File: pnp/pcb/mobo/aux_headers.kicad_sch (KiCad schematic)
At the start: 1 part, among them J21 qwiic

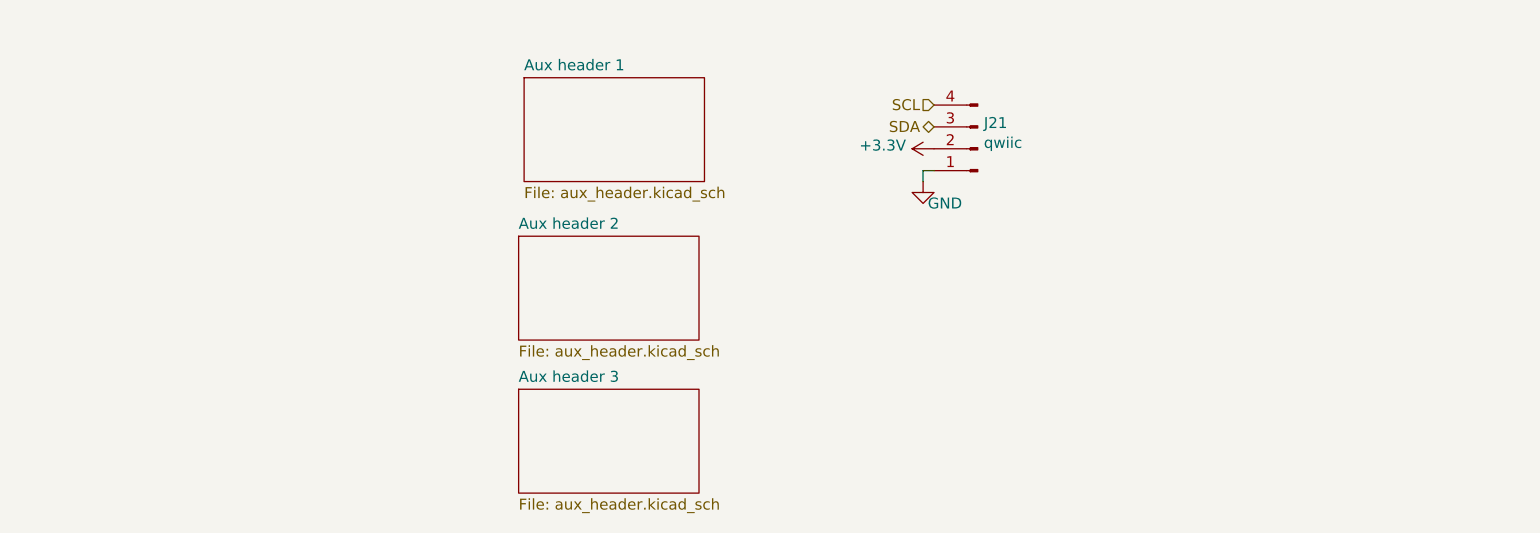
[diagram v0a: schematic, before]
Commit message: All sheets cleaned up
All symbols and their fields are now neatly organized.

All hierarchical pins are already imported,
except for the microcontroller sheet.
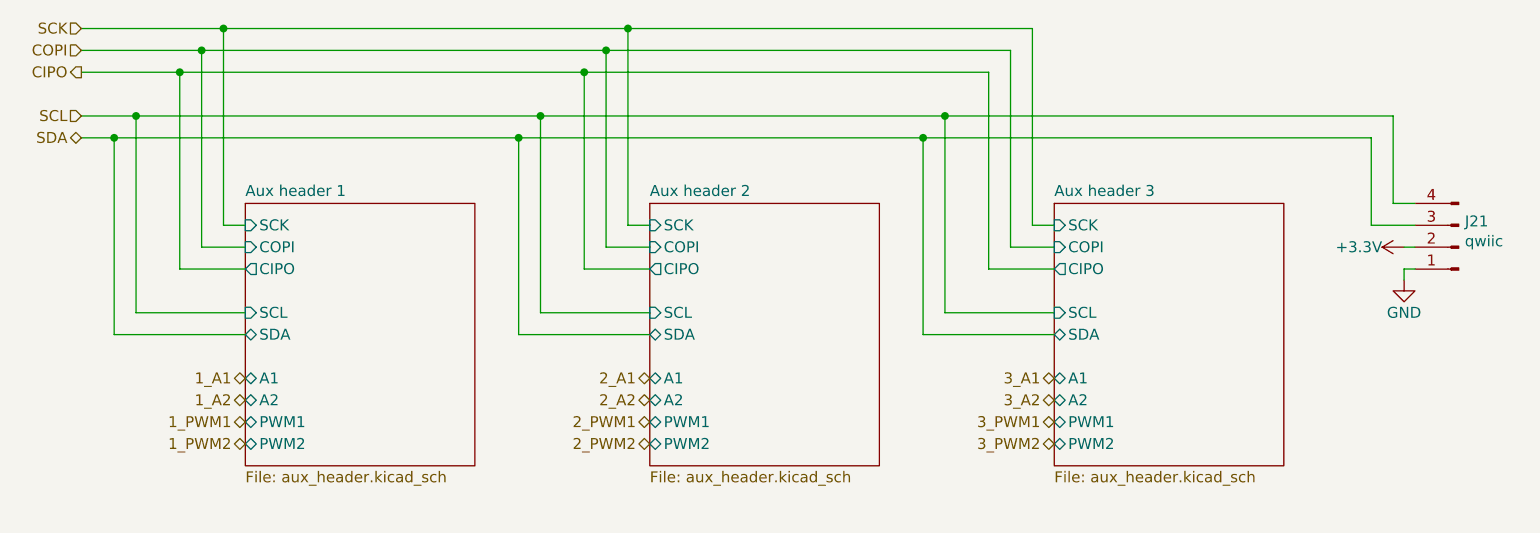
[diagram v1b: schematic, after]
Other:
- sheet Aux header 1 ports: added A1, A2, CIPO, COPI, PWM1, PWM2, SCK, SCL, SDA; removed none
- sheet Aux header 2 ports: added A1, A2, CIPO, COPI, PWM1, PWM2, SCK, SCL, SDA; removed none
- sheet Aux header 3 ports: added A1, A2, CIPO, COPI, PWM1, PWM2, SCK, SCL, SDA; removed none
- moved on the sheet: J21

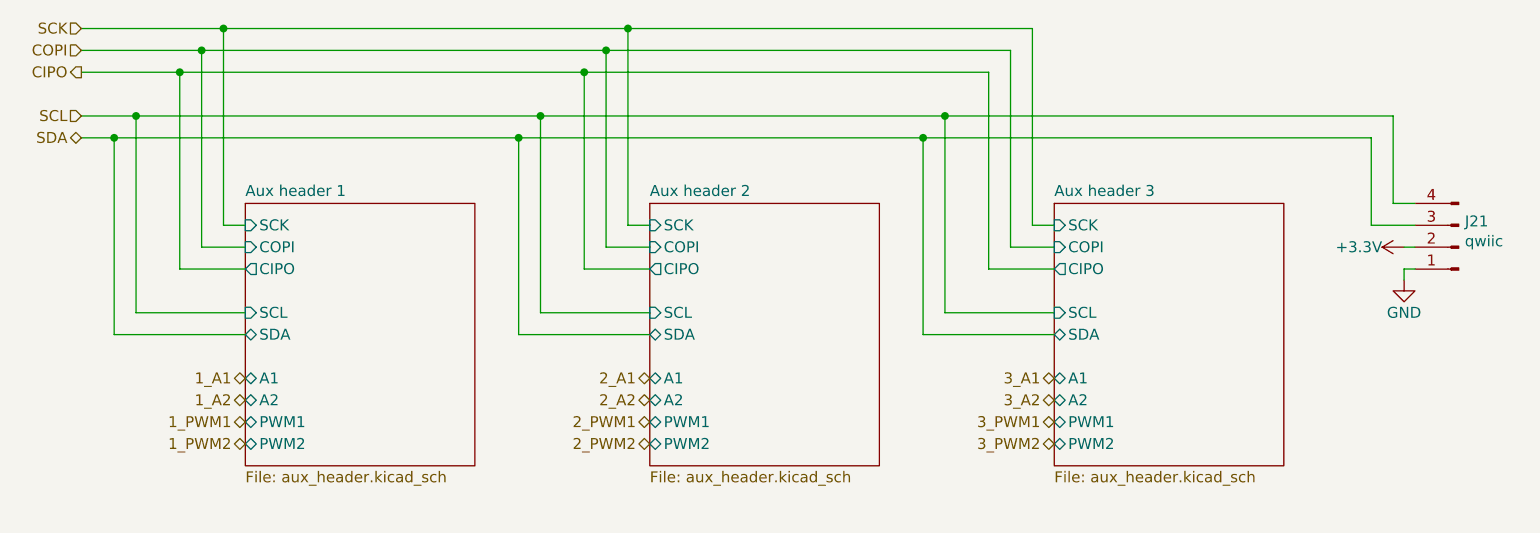
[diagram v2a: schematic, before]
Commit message: moving mobo-rev04b0 into mobo-rev04 branch from old repo
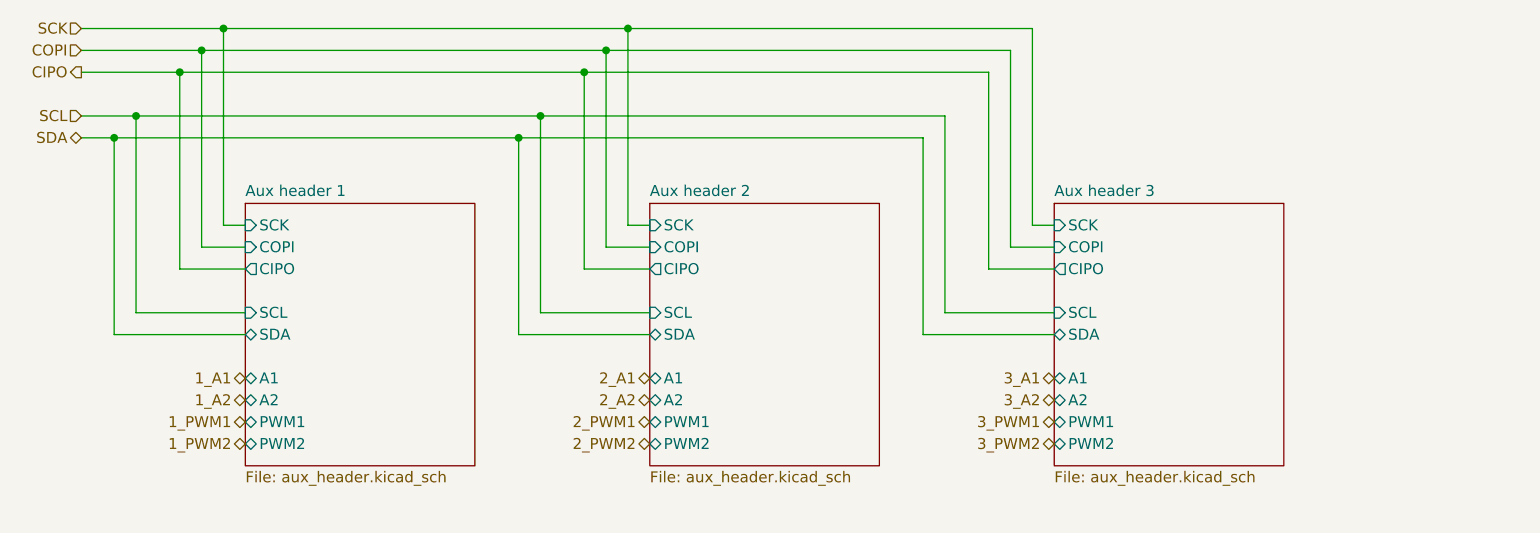
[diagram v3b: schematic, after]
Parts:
- removed J21: qwiic, Connector_JST:JST_SH_BM04B-SRSS-TB_1x04-1MP_P1.00mm_Vertical, symbol Connector:Conn_01x04_Male
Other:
- company: (none) -> Opulo
- title: Output -> LumenPnP Motherboard
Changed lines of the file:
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@@
   (paper "A4")
   (title_block
-    (title "Output")
+    (title "LumenPnP Motherboard")
     (date "2022-03-29")
     (rev "003")
-  )
-  (junction (at 171.45 81.28) (diameter 0) (color 0 0 0 0)
+    (company "Opulo")
   )
   (junction (at 85.09 73.66) (diameter 0) (color 0 0 0 0)
@@
   (junction (at 90.17 68.58) (diameter 0) (color 0 0 0 0)
   )
-  (junction (at 173.99 78.74) (diameter 0) (color 0 0 0 0)
-  )
   (wire (pts (xy 90.17 91.44) (xy 90.17 68.58))
     (stroke (width 0) (type default) (color 0 0 0 0))
@@
     (stroke (width 0) (type default) (color 0 0 0 0))
   )
-  (wire (pts (xy 227.33 97.79) (xy 227.33 96.52))
-    (stroke (width 0) (type default) (color 0 0 0 0))
-  )
   (wire (pts (xy 90.17 91.44) (xy 92.71 91.44))
     (stroke (width 0) (type default) (color 0 0 0 0))
@@
     (stroke (width 0) (type default) (color 0 0 0 0))
   )
-  (wire (pts (xy 226.06 88.9) (xy 226.06 78.74))
-    (stroke (width 0) (type default) (color 0 0 0 0))
-  )
   (wire (pts (xy 137.16 91.44) (xy 137.16 68.58))
     (stroke (width 0) (type default) (color 0 0 0 0))
@@
     (stroke (width 0) (type default) (color 0 0 0 0))
   )
-  (wire (pts (xy 228.6 88.9) (xy 226.06 88.9))
-    (stroke (width 0) (type default) (color 0 0 0 0))
-  )
-  (wire (pts (xy 173.99 78.74) (xy 226.06 78.74))
-    (stroke (width 0) (type default) (color 0 0 0 0))
-  )
   (wire (pts (xy 184.15 91.44) (xy 184.15 68.58))
     (stroke (width 0) (type default) (color 0 0 0 0))
@@
     (stroke (width 0) (type default) (color 0 0 0 0))
   )
-  (wire (pts (xy 171.45 81.28) (xy 223.52 81.28))
-    (stroke (width 0) (type default) (color 0 0 0 0))
-  )
   (wire (pts (xy 132.08 96.52) (xy 132.08 73.66))
     (stroke (width 0) (type default) (color 0 0 0 0))
@@
     (stroke (width 0) (type default) (color 0 0 0 0))
   )
-  (wire (pts (xy 227.33 93.98) (xy 228.6 93.98))
-    (stroke (width 0) (type default) (color 0 0 0 0))
-  )
   (wire (pts (xy 90.17 68.58) (xy 137.16 68.58))
     (stroke (width 0) (type default) (color 0 0 0 0))
@@
     (stroke (width 0) (type default) (color 0 0 0 0))
   )
-  (wire (pts (xy 227.33 96.52) (xy 228.6 96.52))
-    (stroke (width 0) (type default) (color 0 0 0 0))
-  )
-  (wire (pts (xy 223.52 91.44) (xy 228.6 91.44))
-    (stroke (width 0) (type default) (color 0 0 0 0))
-  )
   (wire (pts (xy 127 101.6) (xy 127 78.74))
     (stroke (width 0) (type default) (color 0 0 0 0))
@@
     (stroke (width 0) (type default) (color 0 0 0 0))
   )
-  (wire (pts (xy 223.52 81.28) (xy 223.52 91.44))
-    (stroke (width 0) (type default) (color 0 0 0 0))
-  )
   (wire (pts (xy 134.62 93.98) (xy 134.62 71.12))
     (stroke (width 0) (type default) (color 0 0 0 0))
@@
     (effects (font (size 1.27 1.27)) (justify right))
   )
-  (symbol (lib_id "Connector:Conn_01x04_Male") (at 233.68 93.98 180) (unit 1)
-    (in_bom yes) (on_board yes)
-    (property "Reference" "J21" (id 0) (at 234.3912 90.9828 0)
-      (effects (font (size 1.27 1.27)) (justify right))
-    )
-    (property "Value" "qwiic" (id 1) (at 234.3912 93.2942 0)
-      (effects (font (size 1.27 1.27)) (justify right))
-    )
-    (property "Footprint" "Connector_JST:JST_SH_BM04B-SRSS-TB_1x04-1MP_P1.00mm_Vertical" (id 2) (at 233.68 93.98 0)
-      (effects (font (size 1.27 1.27)) hide)
-    )
-    (property "Datasheet" "" (id 3) (at 233.68 93.98 0)
-      (effects (font (size 1.27 1.27)) hide)
-    )
-    (property "LCSC" "C145961" (id 4) (at 233.68 93.98 0)
-      (effects (font (size 1.27 1.27)) hide)
-    )
-    (property "Config" "+qwiic" (id 5) (at 233.68 93.98 0)
-      (effects (font (size 1.27 1.27)) hide)
-    )
-    (pin "1")
-    (pin "2")
-    (pin "3")
-    (pin "4")
-  )
-  (symbol (lib_id "power:GND") (at 227.33 97.79 0) (unit 1)
-    (in_bom yes) (on_board yes)
-    (property "Reference" "#PWR0185" (id 0) (at 227.33 104.14 0)
-      (effects (font (size 1.27 1.27)) hide)
-    )
-    (property "Value" "GND" (id 1) (at 227.33 101.6 0))
-    (property "Footprint" "" (id 2) (at 227.33 97.79 0)
-      (effects (font (size 1.27 1.27)) hide)
-    )
-    (property "Datasheet" "" (id 3) (at 227.33 97.79 0)
-      (effects (font (size 1.27 1.27)) hide)
-    )
-    (pin "1")
-  )
-  (symbol (lib_id "power:+3.3V") (at 227.33 93.98 90) (unit 1)
-    (in_bom yes) (on_board yes)
-    (property "Reference" "#PWR0186" (id 0) (at 231.14 93.98 0)
-      (effects (font (size 1.27 1.27)) hide)
-    )
-    (property "Value" "+3.3V" (id 1) (at 224.79 93.98 90)
-      (effects (font (size 1.27 1.27)) (justify left))
-    )
-    (property "Footprint" "" (id 2) (at 227.33 93.98 0)
-      (effects (font (size 1.27 1.27)) hide)
-    )
-    (property "Datasheet" "" (id 3) (at 227.33 93.98 0)
-      (effects (font (size 1.27 1.27)) hide)
-    )
-    (pin "1")
-  )
   (sheet (at 92.71 88.9) (size 26.67 30.48) (fields_autoplaced)
